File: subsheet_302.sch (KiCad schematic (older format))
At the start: 32 parts, among them J302 Internal FDD Power, J303 Internal FDD Port, J304 DIN-14S — External FDD Port, U301 WD1772_FLOPPY_DISK_CONTROLLER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, U305 7406_PHY

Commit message: Removed T-filters
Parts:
- removed L300, L301, L302, L303, L304, L305, L306, L307, L308, L309, L310, L311: EMI_Filter_LCL, commons_passives_THT:Passive_THT_EMI_filter_W5.08mm_L7.62mm, symbol Device:EMI_Filter_LCL
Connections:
- net labels removed: ext_fdc_1, ext_fdc_10, ext_fdc_11, ext_fdc_12, ext_fdc_13, ext_fdc_14, ext_fdc_2, ext_fdc_4, ext_fdc_5, ext_fdc_6, ext_fdc_8, ext_fdc_9
- wire segments 162 -> 142
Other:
- moved on the sheet: J302, J303, J304, R302, W300, W301

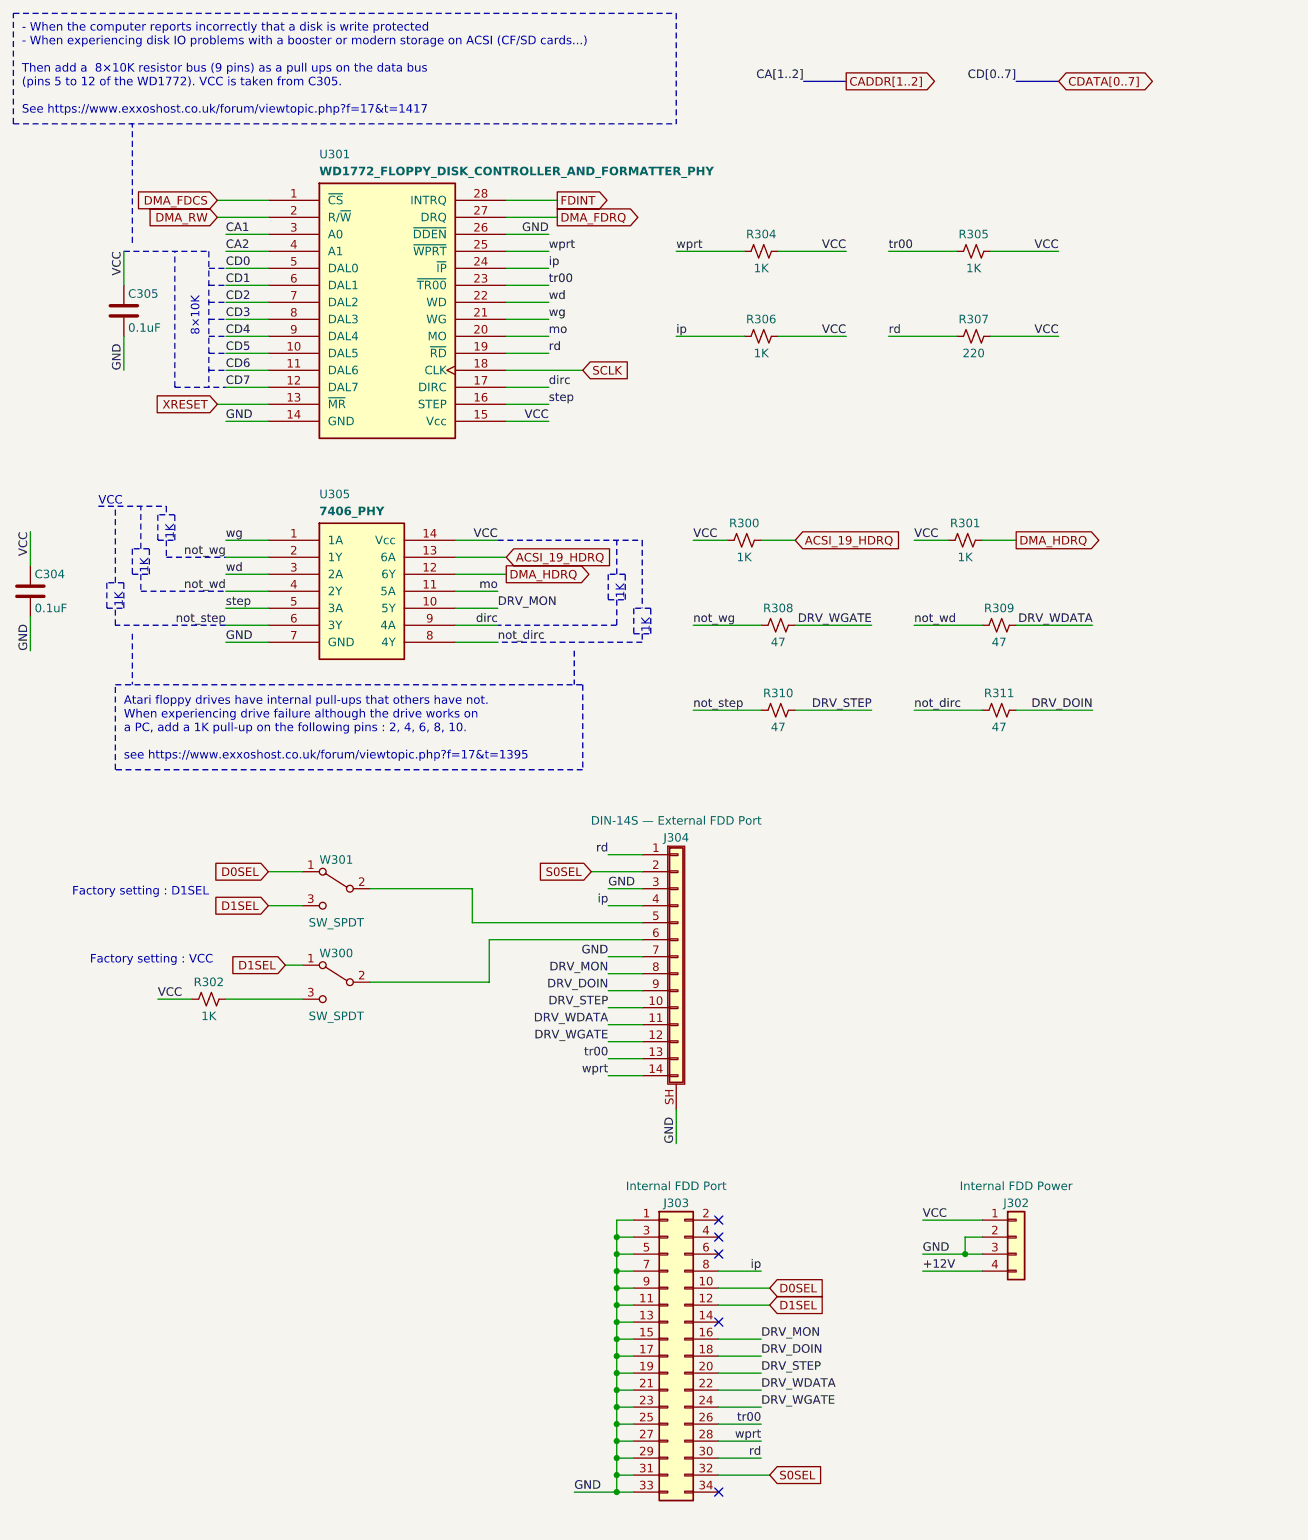
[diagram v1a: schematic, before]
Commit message: Resolves #1 : Use 4-resistor packs wherever it is possible
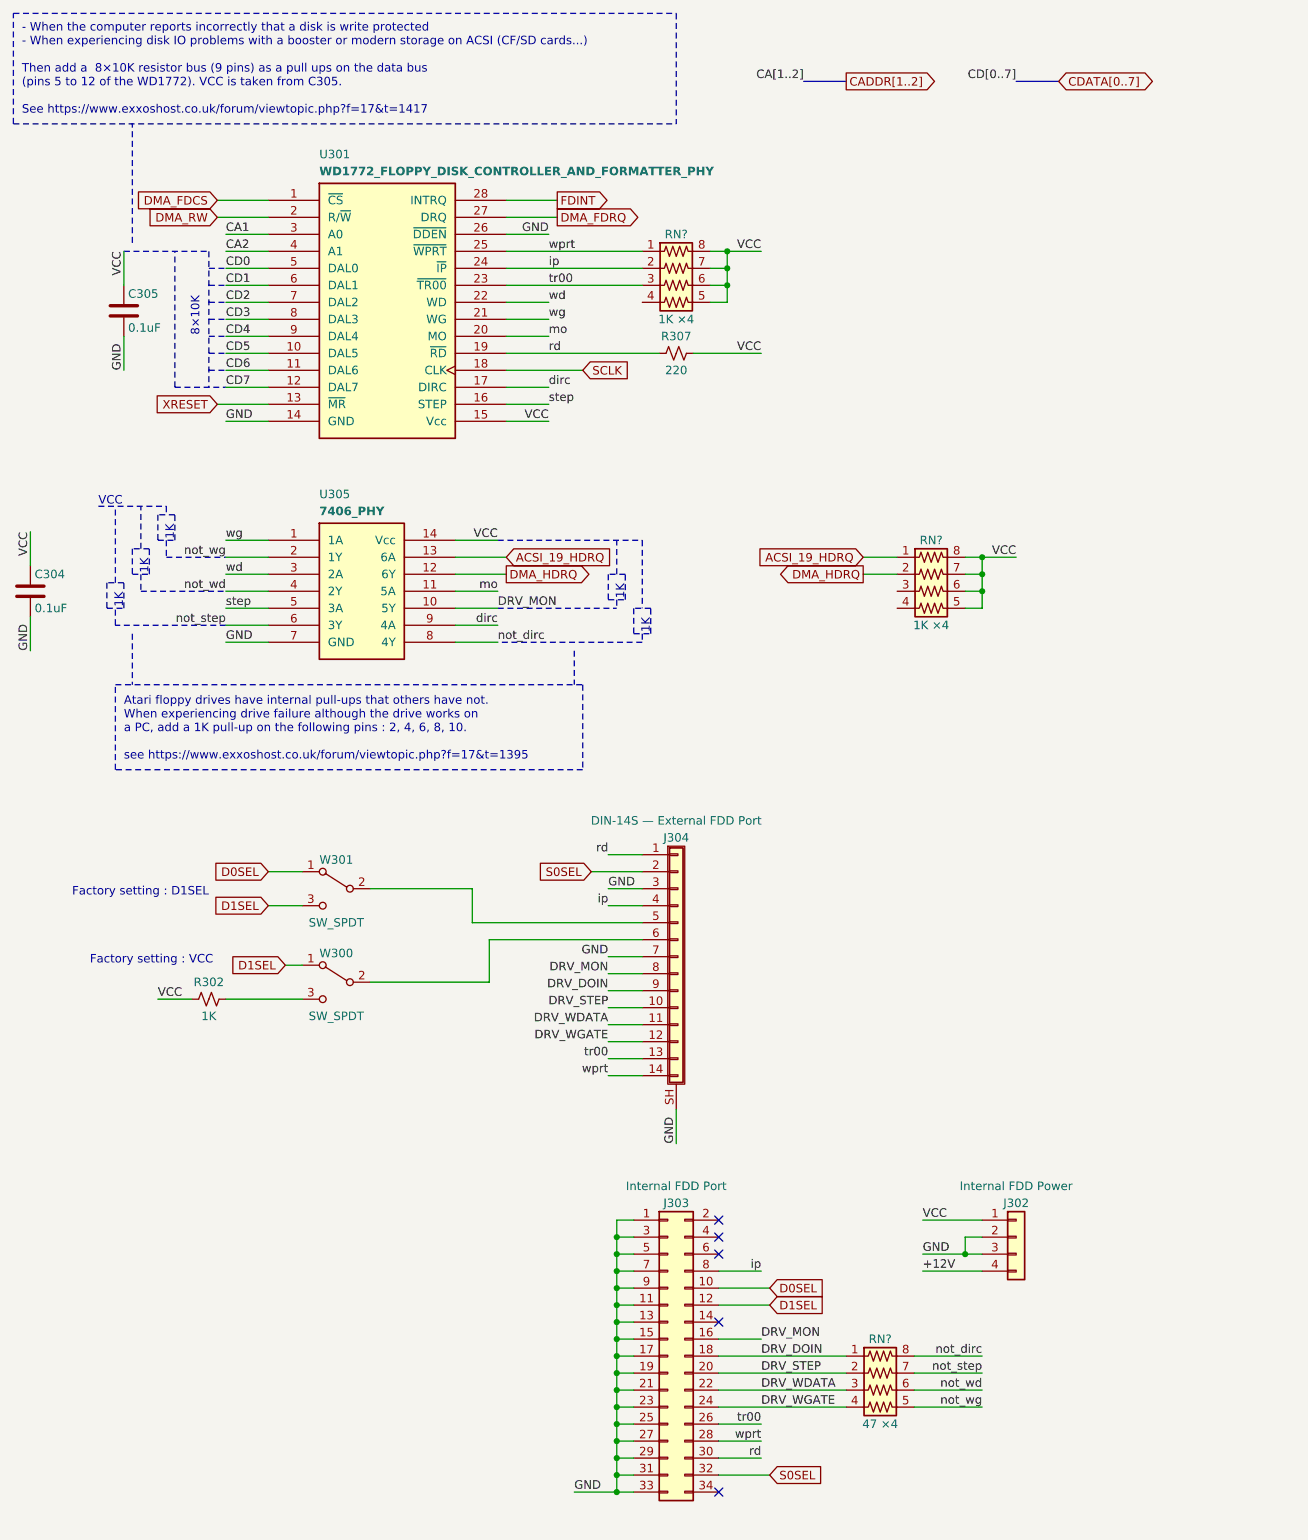
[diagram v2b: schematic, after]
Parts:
- removed R300, R301, R304, R305, R306: 1K, commons_passives_THT:Passive_THT_resistor_W2.54mm_L12.70mm, symbol Device:R_Small_US
- removed R308, R309, R310, R311: 47, commons_passives_THT:Passive_THT_resistor_W2.54mm_L12.70mm, symbol Device:R_Small_US
- added RN?: 47 ×4, symbol custom_passives:R_Pack04_US
- added RN? (x2): 1K ×4, symbol custom_passives:R_Pack04_US
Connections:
- net ACSI_19_HDRQ: now also RN?.1 (R1.1)
- net DMA_HDRQ: now also RN?.2 (R2.1)
- net DRV_DOIN: now also RN?.1 (R1.1)
- net DRV_STEP: now also RN?.2 (R2.1)
- net DRV_WDATA: now also RN?.3 (R3.1)
- net DRV_WGATE: now also RN?.4 (R4.1)
- net VCC: now also RN?.5 (R4.2), RN?.5 (R4.2), RN?.6 (R3.2), RN?.6 (R3.2), RN?.7 (R2.2), RN?.7 (R2.2), RN?.8 (R1.2), RN?.8 (R1.2)
- net ip: now also RN?.2 (R2.1)
- net not_dirc: now also RN?.8 (R1.2)
- net not_step: now also RN?.7 (R2.2)
- net not_wd: now also RN?.6 (R3.2)
- net not_wg: now also RN?.5 (R4.2)
- net tr00: now also RN?.3 (R3.1)
- net wprt: now also RN?.1 (R1.1)
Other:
- moved on the sheet: R307

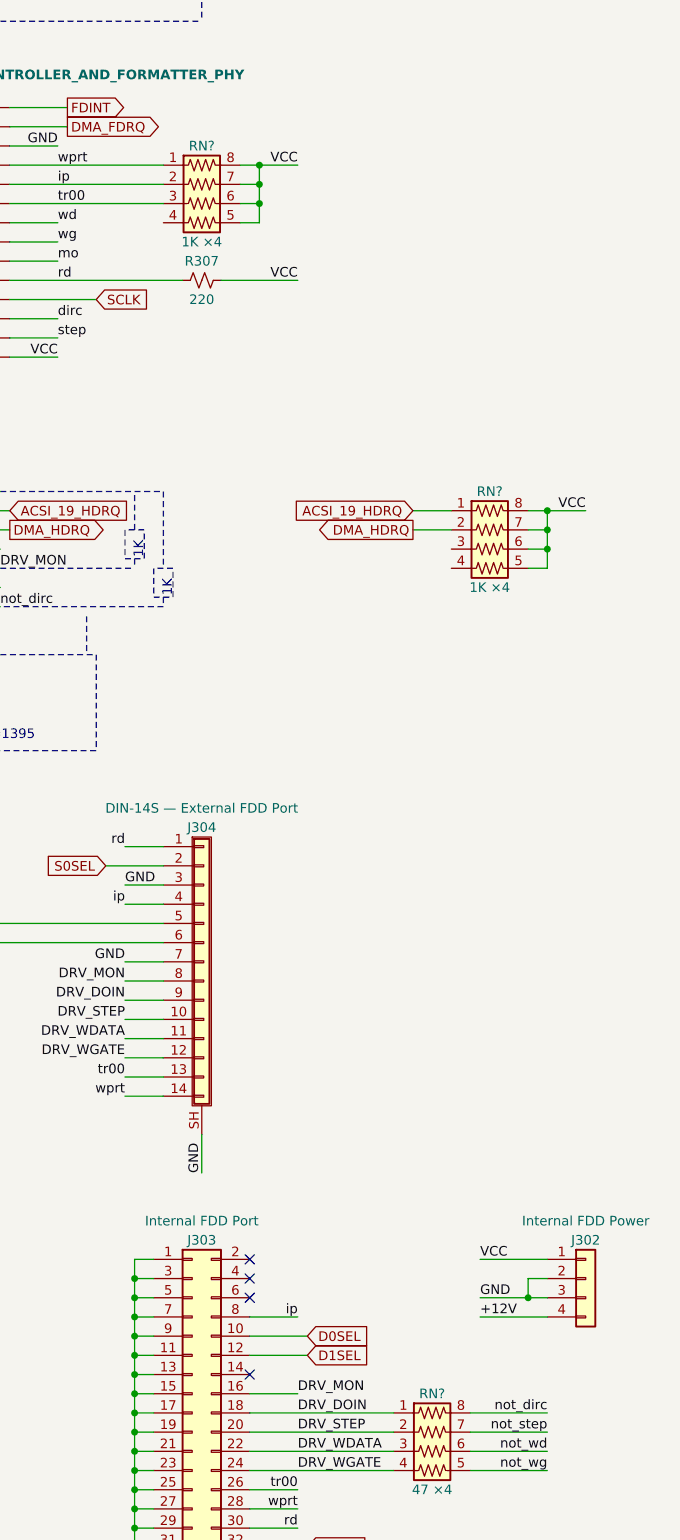
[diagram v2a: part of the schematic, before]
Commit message: annotate resistor networks and mark unused pins as unconnected
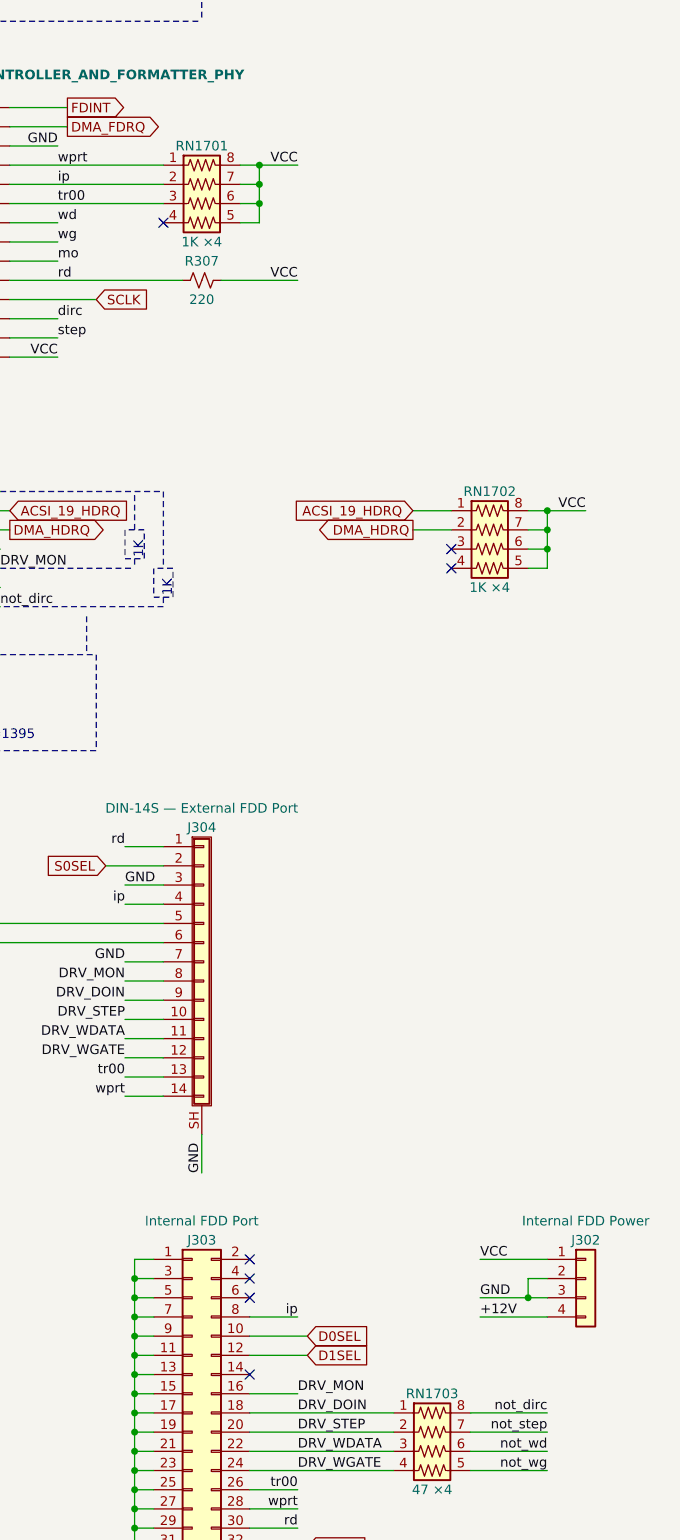
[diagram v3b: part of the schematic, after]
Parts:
- gave numbers to parts that had none: 3
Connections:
- no-connect marks 5 -> 8
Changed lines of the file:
@@
 	3300 5950 3300 5750
 $Comp
-L custom_passives:R_Pack04_US RN?
+L custom_passives:R_Pack04_US RN1703
 U 1 1 620C85E3
 P 5700 8700
-F 0 "RN?" V 5400 8700 50  0000 C CNN
+F 0 "RN1703" V 5400 8700 50  0000 C CNN
 F 1 "47 ×4" V 5900 8700 50  0000 C CNN
 F 2 "" V 5975 8700 50  0001 C CNN
@@
 	4150 4050 4150 4100
 $Comp
-L custom_passives:R_Pack04_US RN?
+L custom_passives:R_Pack04_US RN1701
 U 1 1 622098CD
 P 4500 2200
-F 0 "RN?" V 4200 2200 50  0000 C CNN
+F 0 "RN1701" V 4200 2200 50  0000 C CNN
 F 1 "1K ×4" V 4700 2200 50  0000 C CNN
 F 2 "" V 4775 2200 50  0001 C CNN
@@
 	3500 2600 4400 2600
 $Comp
-L custom_passives:R_Pack04_US RN?
+L custom_passives:R_Pack04_US RN1702
 U 1 1 6225DB28
 P 6000 4000
-F 0 "RN?" V 5700 4000 50  0000 C CNN
+F 0 "RN1702" V 5700 4000 50  0000 C CNN
 F 1 "1K ×4" V 6200 4000 50  0000 C CNN
 F 2 "" V 6275 4000 50  0001 C CNN
@@
 Wire Wire Line
 	6300 3900 6300 3800
+NoConn ~ 5800 4000
+NoConn ~ 5800 4100
+NoConn ~ 4300 2300
 $EndSCHEMATC

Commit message: Resolves #7 : Assign SMD footprints to resistors pack
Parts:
- RN1701, RN1702, RN1703: footprint (none) -> Resistor_SMD:R_Array_Convex_4x0603
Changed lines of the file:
@@
 F 0 "RN1703" V 5400 8700 50  0000 C CNN
 F 1 "47 ×4" V 5900 8700 50  0000 C CNN
-F 2 "" V 5975 8700 50  0001 C CNN
+F 2 "Resistor_SMD:R_Array_Convex_4x0603" V 5975 8700 50  0001 C CNN
 F 3 "~" H 5700 8700 50  0001 C CNN
 	1    5700 8700
@@
 F 0 "RN1701" V 4200 2200 50  0000 C CNN
 F 1 "1K ×4" V 4700 2200 50  0000 C CNN
-F 2 "" V 4775 2200 50  0001 C CNN
+F 2 "Resistor_SMD:R_Array_Convex_4x0603" V 4775 2200 50  0001 C CNN
 F 3 "~" H 4500 2200 50  0001 C CNN
 	1    4500 2200
@@
 F 0 "RN1702" V 5700 4000 50  0000 C CNN
 F 1 "1K ×4" V 6200 4000 50  0000 C CNN
-F 2 "" V 6275 4000 50  0001 C CNN
+F 2 "Resistor_SMD:R_Array_Convex_4x0603" V 6275 4000 50  0001 C CNN
 F 3 "~" H 6000 4000 50  0001 C CNN
 	1    6000 4000

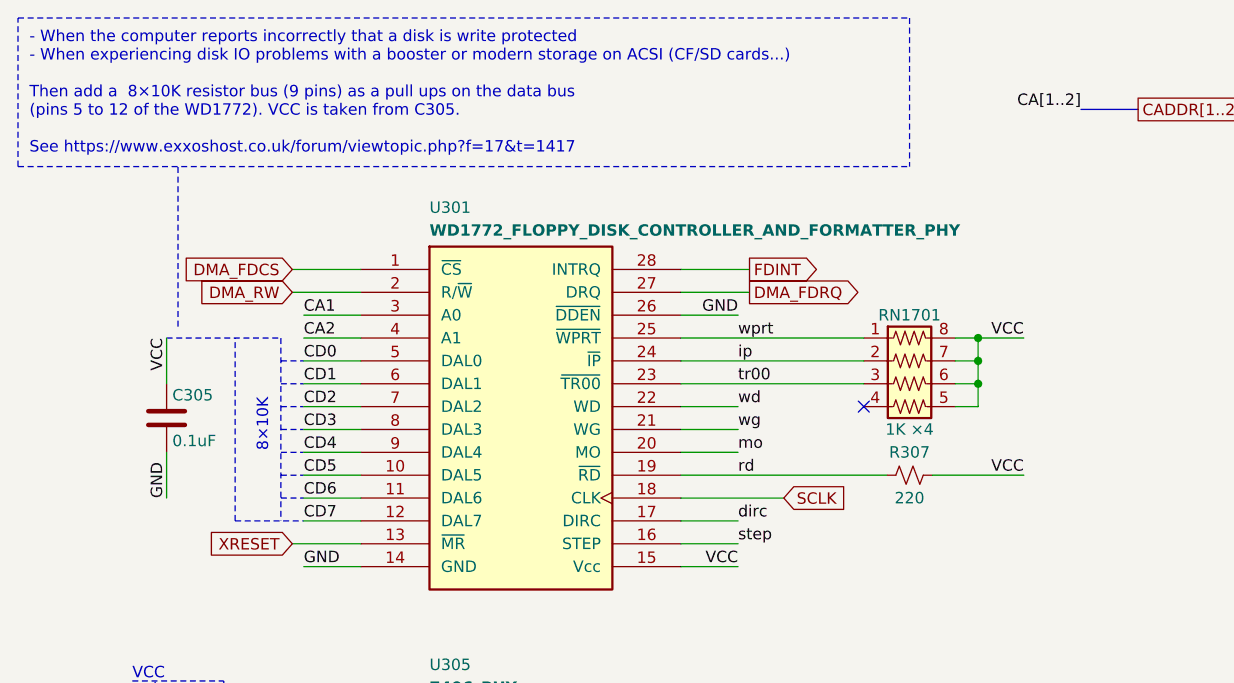
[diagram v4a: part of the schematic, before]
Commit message: Resolves #3 : Apply the DMA Pull up fix on databus
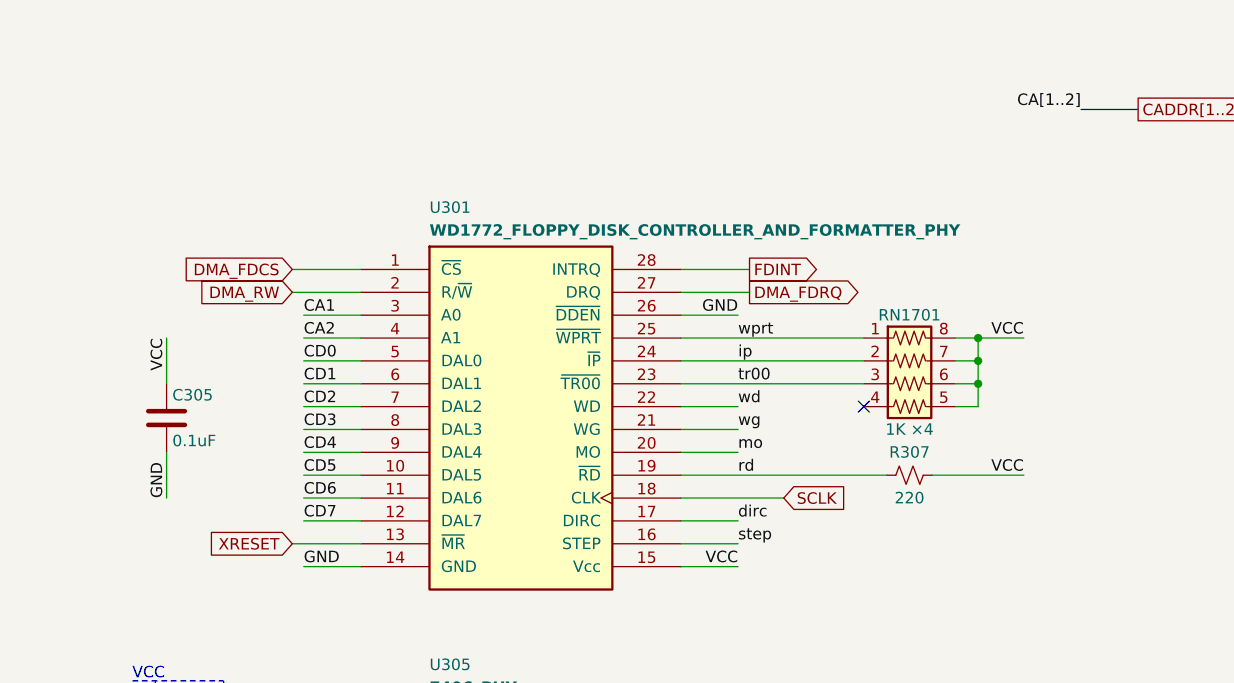
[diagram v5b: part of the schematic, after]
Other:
- note removed: "- When the computer reports incorrectly that a disk is write protected\n- When experiencing disk IO problems with a booster or modern storage on ACSI (CF/SD cards...)\n\nThen add a 8×10K resistor bus (9 pins) as a pull ups on the data bus \n(pins 5 to 12 of the WD1772). VCC is taken from C305.\n\nSee https://www.exxoshost.co.uk/forum/viewtopic.php?f=17&t=1417"
- note removed: "8×10K"
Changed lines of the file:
@@
 Wire Wire Line
 	5950 7700 6300 7700
-Text Notes 650  1200 0    50   ~ 0
-- When the computer reports incorrectly that a disk is write protected\n- When experiencing disk IO problems with a booster or modern storage on ACSI (CF/SD cards...)\n\nThen add a  8×10K resistor bus (9 pins) as a pull ups on the data bus \n(pins 5 to 12 of the WD1772). VCC is taken from C305.\n\nSee https://www.exxoshost.co.uk/forum/viewtopic.php?f=17&t=1417
-Wire Notes Line
-	1750 2000 1750 2800
-Wire Notes Line
-	1550 2800 1550 2000
-Wire Notes Line
-	1250 2000 1750 2000
-Wire Notes Line
-	1750 2100 1850 2100
-Wire Notes Line
-	1750 2200 1850 2200
-Wire Notes Line
-	1750 2300 1850 2300
-Wire Notes Line
-	1750 2400 1850 2400
-Wire Notes Line
-	1750 2500 1850 2500
-Wire Notes Line
-	1750 2600 1850 2600
-Wire Notes Line
-	1750 2700 1850 2700
-Wire Notes Line
-	1550 2800 1850 2800
-Text Notes 1700 2500 1    50   ~ 0
-8×10K
-Wire Notes Line
-	1300 1950 1300 1250
 Text Notes 1250 5000 0    50   ~ 0
 Atari floppy drives have internal pull-ups that others have not.\nWhen experiencing drive failure although the drive works on\na PC, add a 1K pull-up on the following pins : 2, 4, 6, 8, 10.\n\nsee https://www.exxoshost.co.uk/forum/viewtopic.php?f=17&t=1395
@@
 Wire Notes Line
 	3900 4350 3900 4550
-Wire Notes Line
-	600  1250 600  600
-Wire Notes Line
-	600  600  4500 600
-Wire Notes Line
-	4500 600  4500 1250
-Wire Notes Line
-	600  1250 4500 1250
 Wire Wire Line
 	3400 6050 3400 6300
